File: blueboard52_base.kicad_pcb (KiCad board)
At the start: 2 copper layers, 42.2 x 43.1 mm, 19 parts, among them J1 Conn_East, J2 Conn_West, J3 Conn_South, J4 VCC, J5 GND, J6 NFC, SW1 RST, SW2 DFU, U1 E73-2G4M04S-52832

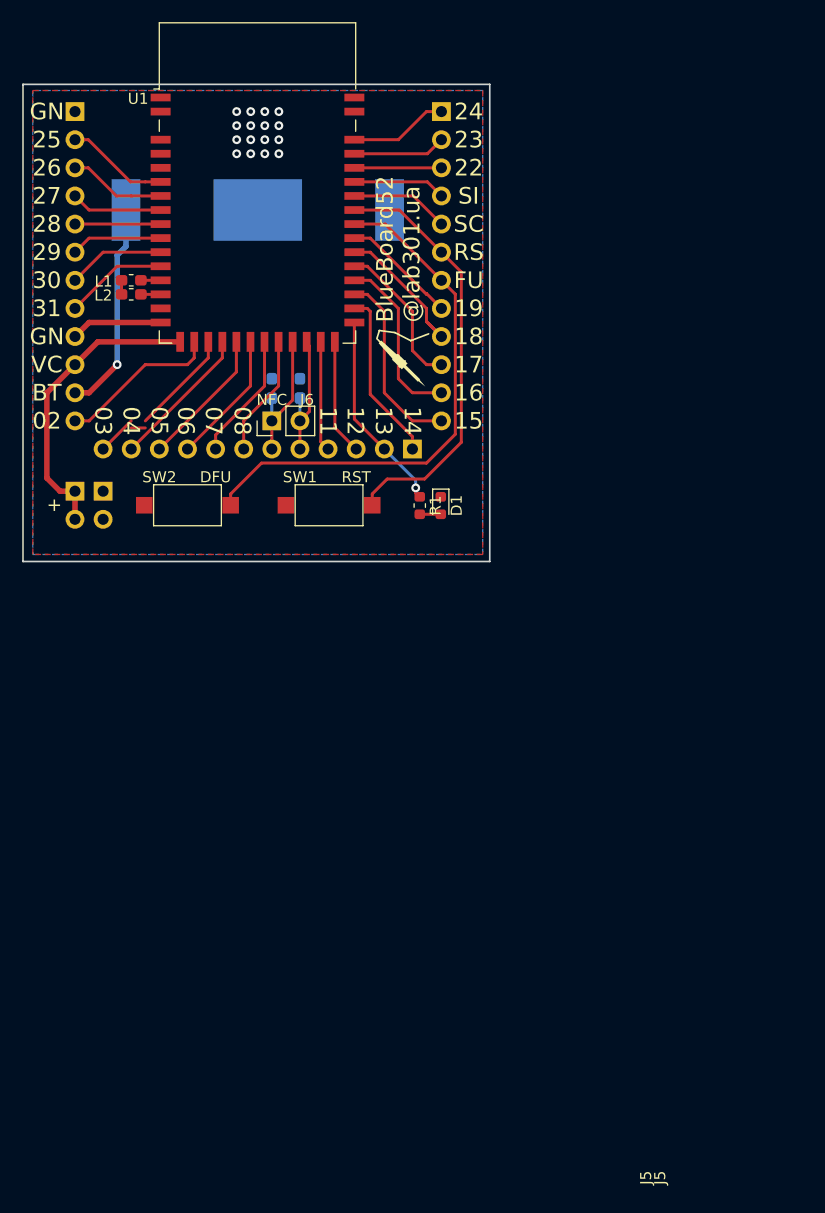
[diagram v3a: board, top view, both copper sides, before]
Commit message: v0.2.2 - Visual cleanup
- Reviewed ground planes once again.
  Return current from external connector now flows on the top layer
  and from the battery - on the bottom copper layer.
- Listed main acronims for board pins
- Added a note for Battery-VCC jumper
- Other small changes
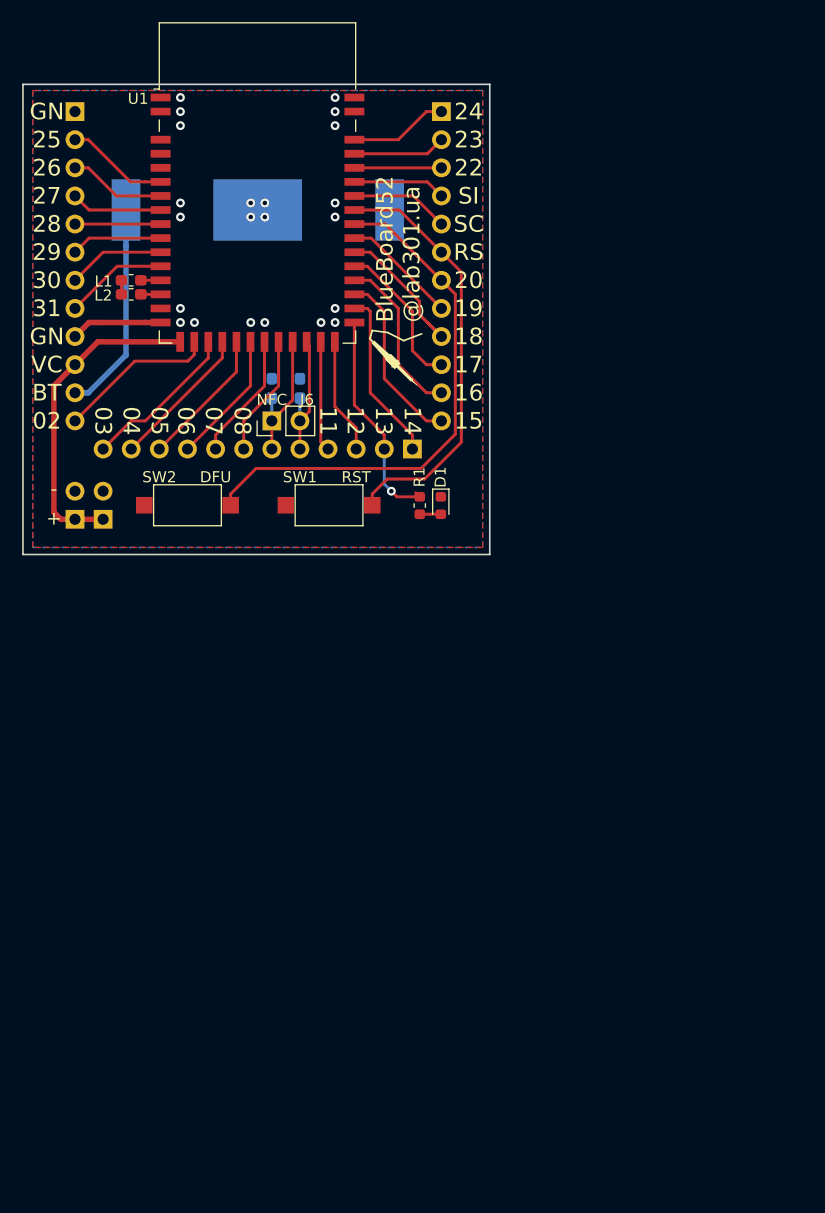
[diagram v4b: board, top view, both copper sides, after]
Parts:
- removed ? (x2): , 
- removed the svg2mod at (85.9, 53.8)
- added REF**: OSHW-Logo_5.7x6mm_SilkScreen, Symbol:OSHW-Logo_5.7x6mm_SilkScreen, B.Cu at (84.0, 67.1)
- added svg2mod: G***, lab301_library:lab301i_logo, B.Cu at (90.3, 66.5)
- added svg2mod: G***, lab301_library:lab301i_logo, F.Cu at (85.2, 53.8)
- J4: value VCC -> PWR
- J5: value GND -> PWR
- moved J4 2.54 mm to (56.7, 68.4), turned to 0 degrees
- moved J5 2.54 mm to (59.2, 68.4), turned to 0 degrees
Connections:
- J4 pad 2: VCC -> GND
- J5 pad 1: GND -> VCC
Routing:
- net VCC: track 27.2 -> 29.2 mm
- net /USER_LED1: track 18.2 -> 19.9 mm
- net /P0.16: track 15.8 -> 15.0 mm
- net /P0.15: track 16.9 -> 16.2 mm
- net +BATT: track 19.2 -> 19.1 mm, vias 1 -> 0
- net GND: vias 16 -> 22
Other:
- board size 42.2 x 43.1 mm -> 42.2 x 42.5 mm
- board text added: "-"
- board text added: "20"
- board text added: "CR2032 3V"
- board text added: "GN: Ground SI: SWDIO, Data SC: SWDCLK, Clock RS: Reset VC: VCC"
- board text added: "Short pins for battery power"
- board text added: "v0.2.2 git.io/JvDuP"
- board text removed: "FU"
- board text removed: "v0.2.1 git.io/JvDsQ"

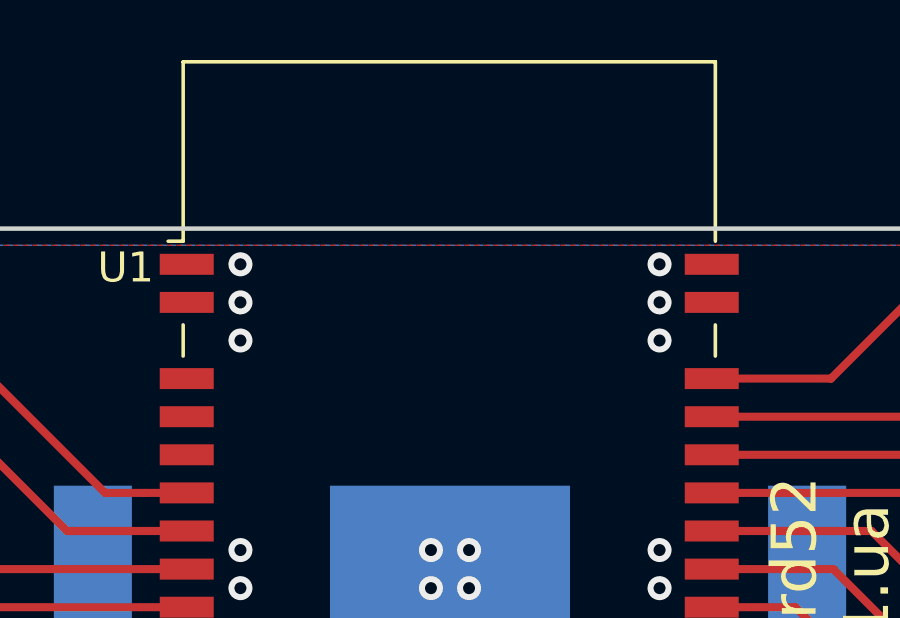
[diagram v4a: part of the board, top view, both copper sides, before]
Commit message: Specified location for manufacturing number
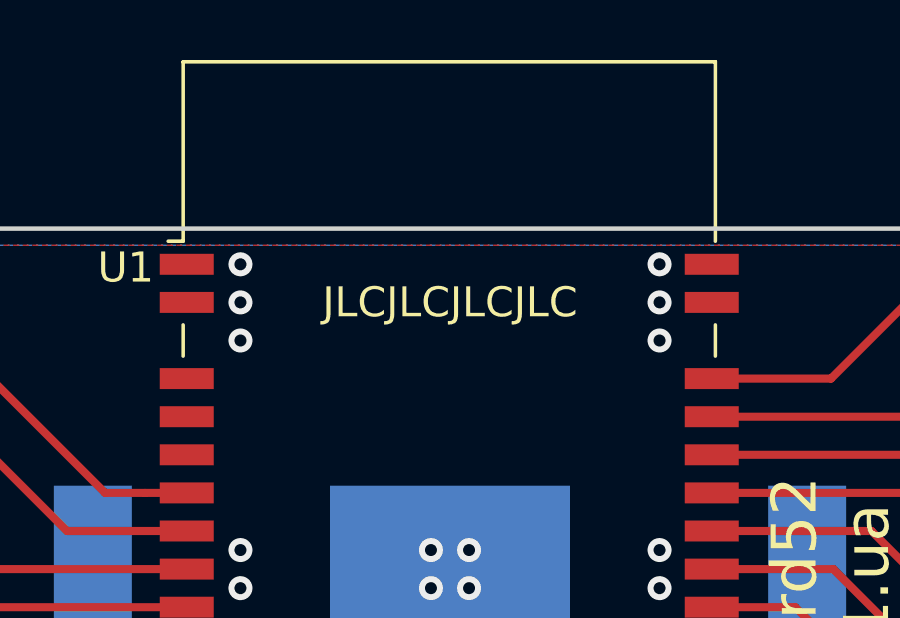
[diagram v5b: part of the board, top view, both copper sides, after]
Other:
- board text added: "JLCJLCJLCJLC"
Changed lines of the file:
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@@
   (general
     (thickness 1.6)
-    (drawings 84)
+    (drawings 85)
     (tracks 160)
     (zones 0)
@@
     (add_net "Net-(L1-Pad2)")
     (add_net "Net-(L2-Pad2)")
-    (add_net "Net-(U1-Pad14)")
-    (add_net "Net-(U1-Pad3)")
-    (add_net "Net-(U1-Pad4)")
   )
   (net_class Power ""
@@
     )
   )
+  (gr_text JLCJLCJLCJLC (at 73.17 31.54) (layer F.SilkS)
+    (effects (font (size 1 1) (thickness 0.15)))
+  )
   (gr_text "GN: Ground\nSI: SWDIO, Data\nSC: SWDCLK, Clock\nRS: Reset\nVC: VCC" (at 88.41 53.13) (layer B.SilkS)
     (effects (font (size 1 1) (thickness 0.15)) (justify left mirror))
@@
   (gr_line (start 94.125 29.08) (end 51.96 29.08) (layer Edge.Cuts) (width 0.15))
   (gr_line (start 94.125 71.545) (end 94.125 29.08) (layer Edge.Cuts) (width 0.15))
+  (segment (start 64.395 46.78) (end 62.615 46.78) (width 0.27) (layer F.Cu) (net 1))
+  (segment (start 62.615 48.05) (end 64.395 48.05) (width 0.27) (layer F.Cu) (net 2))
+  (segment (start 58.72 52.34) (end 56.66 54.4) (width 0.5) (layer F.Cu) (net 3))
+  (segment (start 66.16 52.34) (end 58.72 52.34) (width 0.5) (layer F.Cu) (net 3))
+  (segment (start 55.39 68.37) (end 56.66 68.37) (width 0.5) (layer F.Cu) (net 3))
+  (segment (start 59.2 68.37) (end 56.66 68.37) (width 0.5) (layer F.Cu) (net 3))
+  (segment (start 54.755 56.305) (end 54.755 67.735) (width 0.5) (layer F.Cu) (net 3))
+  (segment (start 56.66 54.4) (end 54.755 56.305) (width 0.5) (layer F.Cu) (net 3))
+  (segment (start 54.755 67.735) (end 55.39 68.37) (width 0.5) (layer F.Cu) (net 3))
+  (segment (start 60.865 46.78) (end 60.865 48.05) (width 0.27) (layer F.Cu) (net 4))
   (via (at 72.535 41.065) (size 0.8) (drill 0.4) (layers F.Cu B.Cu) (net 5))
   (via (at 73.805 41.065) (size 0.8) (drill 0.4) (layers F.Cu B.Cu) (net 5))
   (via (at 73.805 39.795) (size 0.8) (drill 0.4) (layers F.Cu B.Cu) (net 5))
   (via (at 72.535 39.795) (size 0.8) (drill 0.4) (layers F.Cu B.Cu) (net 5))
-  (segment (start 64.395 46.78) (end 62.615 46.78) (width 0.27) (layer F.Cu) (net 1))
-  (segment (start 62.615 48.05) (end 64.395 48.05) (width 0.27) (layer F.Cu) (net 2))
-  (segment (start 58.72 52.34) (end 56.66 54.4) (width 0.5) (layer F.Cu) (net 3))
-  (segment (start 66.16 52.34) (end 58.72 52.34) (width 0.5) (layer F.Cu) (net 3))
-  (segment (start 60.865 46.78) (end 60.865 48.05) (width 0.27) (layer F.Cu) (net 4))
   (via (at 80.155 41.065) (size 0.8) (drill 0.4) (layers F.Cu B.Cu) (net 5))
   (via (at 66.185 49.32) (size 0.8) (drill 0.4) (layers F.Cu B.Cu) (net 5))
@@
   (via (at 80.155 31.54) (size 0.8) (drill 0.4) (layers F.Cu B.Cu) (net 5))
   (via (at 66.185 31.54) (size 0.8) (drill 0.4) (layers F.Cu B.Cu) (net 5))
-  (segment (start 55.39 68.37) (end 56.66 68.37) (width 0.5) (layer F.Cu) (net 3))
-  (segment (start 59.2 68.37) (end 56.66 68.37) (width 0.5) (layer F.Cu) (net 3))
-  (segment (start 54.755 56.305) (end 54.755 67.735) (width 0.5) (layer F.Cu) (net 3))
-  (segment (start 56.66 54.4) (end 54.755 56.305) (width 0.5) (layer F.Cu) (net 3))
-  (segment (start 54.755 67.735) (end 55.39 68.37) (width 0.5) (layer F.Cu) (net 3))
   (segment (start 59.2 50.59) (end 58.565 50.59) (width 0.5) (layer F.Cu) (net 5))
   (segment (start 63.01 50.59) (end 59.2 50.59) (width 0.5) (layer F.Cu) (net 5))
